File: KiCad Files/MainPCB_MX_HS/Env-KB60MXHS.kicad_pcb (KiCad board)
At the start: 2 copper layers, 283 x 126.5 mm, 153 parts, among them J1 Conn_01x04, SW1 EVQPUL, U1 Pico

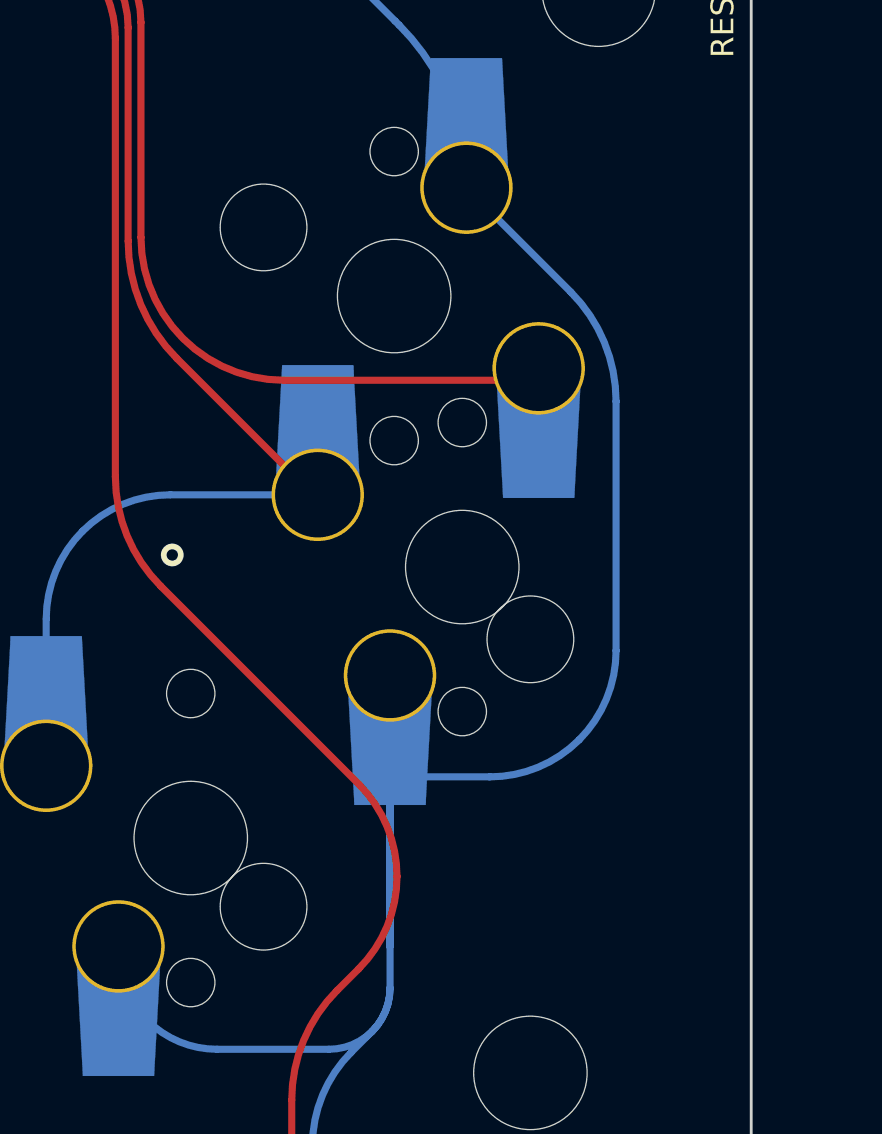
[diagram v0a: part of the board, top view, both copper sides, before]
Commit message: fixed iso enter stabiliser position, validated position of ansi enter, ansi backslash, iso enter, iso right bracket, iso hash key.
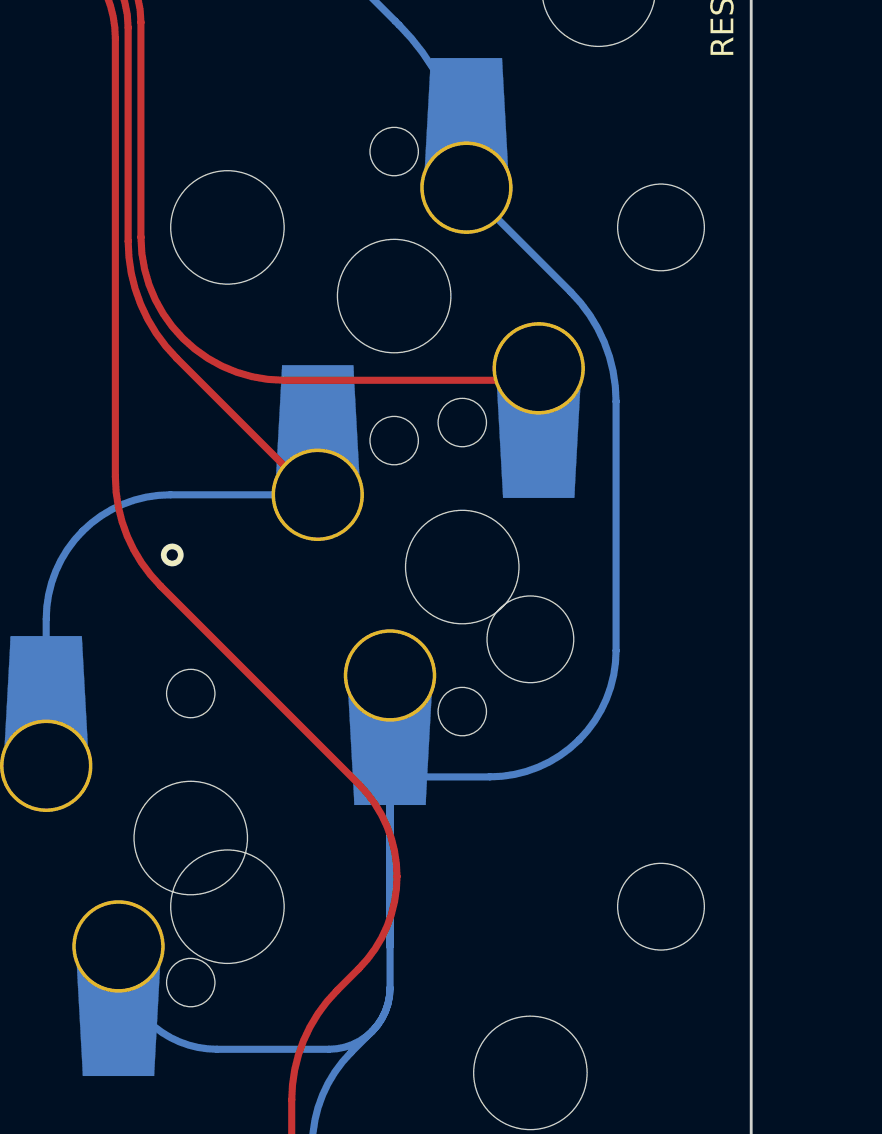
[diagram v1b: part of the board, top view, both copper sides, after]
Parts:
- turned stab4 to -90 degrees
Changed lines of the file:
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@@
 		(fp_arc
 			(start 3.80304 -1.003128)
-			(mid 3.657193 -1.038154)
+			(mid 3.657198 -1.03816)
 			(end 3.532782 -1.121938)
 			(stroke
@@
 	(footprint "Mounting_Keyboard_Stabilizer:Stabilizer_Cherry_MX_2u"
 		(layer "F.Cu")
-		(at 349.84375 103.075 90)
+		(at 349.84375 103.075 -90)
 		(descr "Cherry MX key stabilizer 2u 2.25u 2.5u 2.75u")
 		(tags "Cherry MX key stabilizer 2u 2.25u 2.5u 2.75u")
@@
 		(attr exclude_from_pos_files exclude_from_bom)
 		(fp_line
-			(start -2 0)
-			(end 2 0)
+			(start 0 2.000001)
+			(end 0 -2.000001)
 			(stroke
 				(width 0.1)
@@
 		)
 		(fp_line
-			(start 0 2)
-			(end 0 -2)
+			(start -2.000001 0)
+			(end 2.000001 0)
 			(stroke
 				(width 0.1)
@@
 		)
 		(pad "" np_thru_hole circle
-			(at -11.938 -6.985 90)
+			(at -11.938 -6.985 270)
 			(size 3.048 3.048)
 			(drill 3.048)
 			(layers "*.Cu" "*.Mask")
 		)
-		(pad "" np_thru_hole oval
-			(at -11.925299 9.5 90)
-			(size 4.025896 6.488894)
-			(drill oval 3.9878 6.488894)
-			(layers "F&B.Cu" "*.Mask")
+		(pad "" np_thru_hole circle
+			(at -11.938 8.255 270)
+			(size 3.9878 3.9878)
+			(drill 3.9878)
+			(layers "*.Cu" "*.Mask")
 		)
 		(pad "" np_thru_hole circle
-			(at 11.938 -6.985 90)
+			(at 11.938 -6.985 270)
 			(size 3.048 3.048)
 			(drill 3.048)
 			(layers "*.Cu" "*.Mask")
 		)
-		(pad "" np_thru_hole oval
-			(at 11.938 9.5 90)
-			(size 4.025896 6.488894)
-			(drill oval 3.9878 6.488894)
-			(layers "F&B.Cu" "*.Mask")
+		(pad "" np_thru_hole circle
+			(at 11.938 8.255 270)
+			(size 3.9878 3.9878)
+			(drill 3.9878)
+			(layers "*.Cu" "*.Mask")
 		)
 		(model "${KIPRJMOD}/Switch_Keyboard/packages3d/Mounting_Keyboard_Stabilizer.3dshapes/Stabilizer_Cherry_MX_2u.wrl"

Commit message: removed ground fill to see how it would look with transparent soldermask
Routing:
- net Net-(D_591-A): track 165.8 -> 0.00 mm, vias 1 -> 0
- net Net-(D_590-A): track 124.2 -> 0.00 mm, vias 1 -> 0
- net col7: track 197.4 -> 163.7 mm, vias 1 -> 0
- net col5: track 269.6 -> 240.1 mm, vias 1 -> 0
- net GND: track 0.00 -> 19.3 mm
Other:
- board text removed: "Enjoying the view of my bottom?"
- board text removed: "Frogs are Pog!"
- board text removed: "This is all an elaborate scheme to put words on screens!"
- board text removed: "This space bar doesnt stock milk."
- board text removed: "tyvm Dasky for looking over this board."
